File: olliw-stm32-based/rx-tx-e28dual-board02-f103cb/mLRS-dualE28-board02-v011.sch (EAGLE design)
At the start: 34 parts, among them IC1 STM32F103CB, IC2 NCP1117ST33, IC3 E28-2G4M27S, IC4 74AHC1G86, IC5 74AHC1G86, IC6 E28-2G4M27S, Q1 CSTCE8M00G55-R0

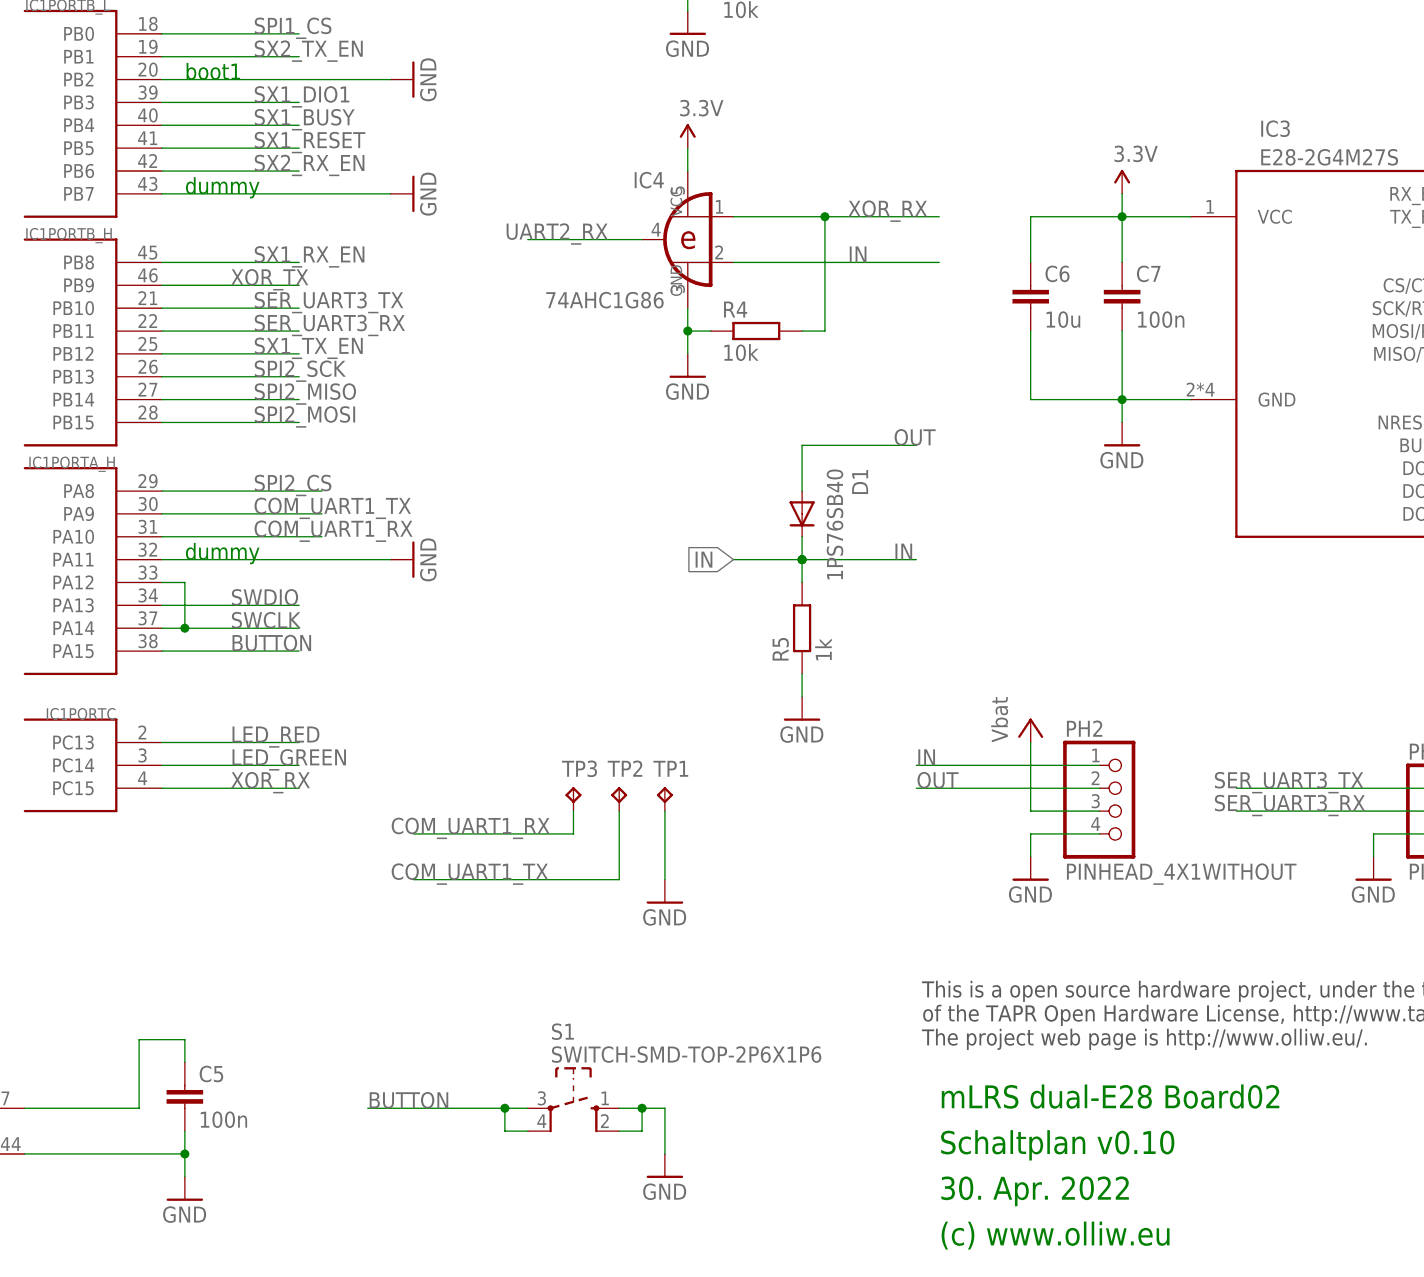
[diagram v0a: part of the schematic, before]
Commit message: rx tx module02 dualE28 F103CB v011, buzzer pad added
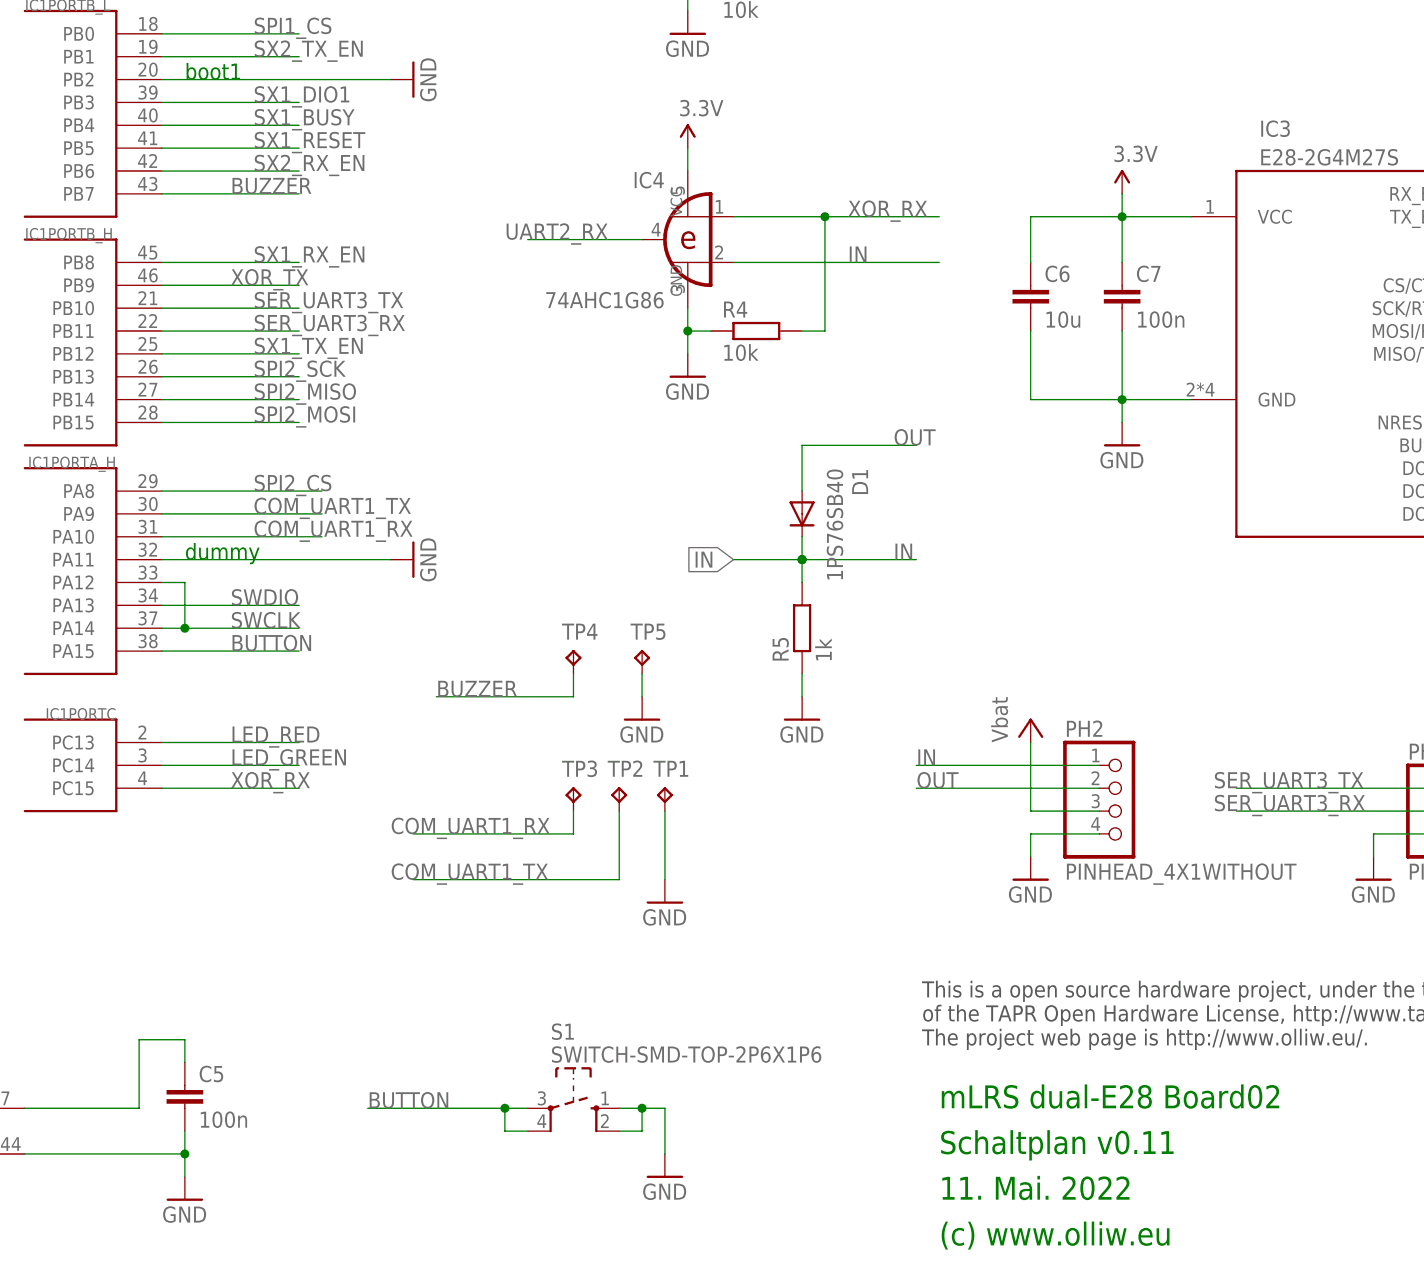
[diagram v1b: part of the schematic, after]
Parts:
- added TP4, TP5: TPTP15R, testpad:TPTP15R
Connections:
- new net BUZZER: IC1PORTB_L.PB7, TP4.TP
- net GND: now also TP5.TP; no longer IC1PORTB_L.PB7
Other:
- note added: "11. Mai. 2022"
- note added: "Schaltplan v0.11"
- note removed: "30. Apr. 2022"
- note removed: "Schaltplan v0.10"
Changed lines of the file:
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@@
 <part name="GND12" library="# supply1" deviceset="GND" device=""/>
 <part name="D1" library="diode" deviceset="DIODE-" device="SOD110-R" value="1PS76SB40"/>
+<part name="GND13" library="# supply1" deviceset="GND" device=""/>
+<part name="TP4" library="testpad" deviceset="TP" device="TP15R" value="TPTP15R"/>
+<part name="TP5" library="testpad" deviceset="TP" device="TP15R" value="TPTP15R"/>
 <part name="GND6" library="# supply1" deviceset="GND" device=""/>
-<part name="GND13" library="# supply1" deviceset="GND" device=""/>
 </parts>
 <sheets>
 <sheet>
 <plain>
-<text x="180.34" y="-38.1" size="2.54" layer="91">30. Apr. 2022</text>
+<text x="180.34" y="-38.1" size="2.54" layer="91">11. Mai. 2022</text>
 <text x="180.34" y="-43.18" size="2.54" layer="91">(c) www.olliw.eu</text>
 <text x="180.34" y="-27.94" size="2.54" layer="91">mLRS dual-E28 Board02</text>
-<text x="180.34" y="-33.02" size="2.54" layer="91">Schaltplan v0.10</text>
+<text x="180.34" y="-33.02" size="2.54" layer="91">Schaltplan v0.11</text>
 <text x="178.435" y="-20.955" size="1.778" layer="97">This is a open source hardware project, under the terms
 of the TAPR Open Hardware License, http://www.tapr.org/ohl.html.
 The project web page is http://www.olliw.eu/.</text>
 <text x="96.52" y="86.36" size="1.778" layer="91">boot1</text>
-<text x="96.52" y="73.66" size="1.778" layer="91">dummy</text>
 <text x="96.52" y="33.02" size="1.778" layer="91">dummy</text>
 </plain>
@@
 <attribute name="VALUE" x="167.8686" y="43.18" size="1.778" layer="96" rot="R270"/>
 </instance>
-<instance part="GND6" gate="1" x="121.92" y="73.66" rot="R90"/>
 <instance part="GND13" gate="1" x="121.92" y="33.02" rot="R90"/>
+<instance part="TP4" gate="G$1" x="139.7" y="22.86"/>
+<instance part="TP5" gate="G$1" x="147.32" y="22.86"/>
+<instance part="GND6" gate="1" x="147.32" y="15.24"/>
 </instances>
 <busses>
@@
 </segment>
 <segment>
-<pinref part="IC1" gate="PORTB_L" pin="PB7"/>
-<pinref part="GND6" gate="1" pin="GND"/>
-<wire x1="93.98" y1="73.66" x2="119.38" y2="73.66" width="0.1524" layer="91"/>
-</segment>
-<segment>
 <pinref part="IC1" gate="PORTA_H" pin="PA11"/>
 <pinref part="GND13" gate="1" pin="GND"/>
 <wire x1="93.98" y1="33.02" x2="119.38" y2="33.02" width="0.1524" layer="91"/>
+</segment>
+<segment>
+<pinref part="TP5" gate="G$1" pin="TP"/>
+<pinref part="GND6" gate="1" pin="GND"/>
+<wire x1="147.32" y1="20.32" x2="147.32" y2="17.78" width="0.1524" layer="91"/>
 </segment>
 </net>
@@
 </segment>
 </net>
+<net name="BUZZER" class="0">
+<segment>
+<pinref part="TP4" gate="G$1" pin="TP"/>
+<wire x1="139.7" y1="20.32" x2="139.7" y2="17.78" width="0.1524" layer="91"/>
+<wire x1="139.7" y1="17.78" x2="124.46" y2="17.78" width="0.1524" layer="91"/>
+<label x="124.46" y="17.78" size="1.778" layer="95"/>
+</segment>
+<segment>
+<pinref part="IC1" gate="PORTB_L" pin="PB7"/>
+<wire x1="93.98" y1="73.66" x2="109.22" y2="73.66" width="0.1524" layer="91"/>
+<label x="101.6" y="73.66" size="1.778" layer="95"/>
+</segment>
+</net>
